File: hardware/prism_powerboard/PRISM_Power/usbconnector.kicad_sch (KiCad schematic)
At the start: 1 part, among them P1 USB_C_Plug

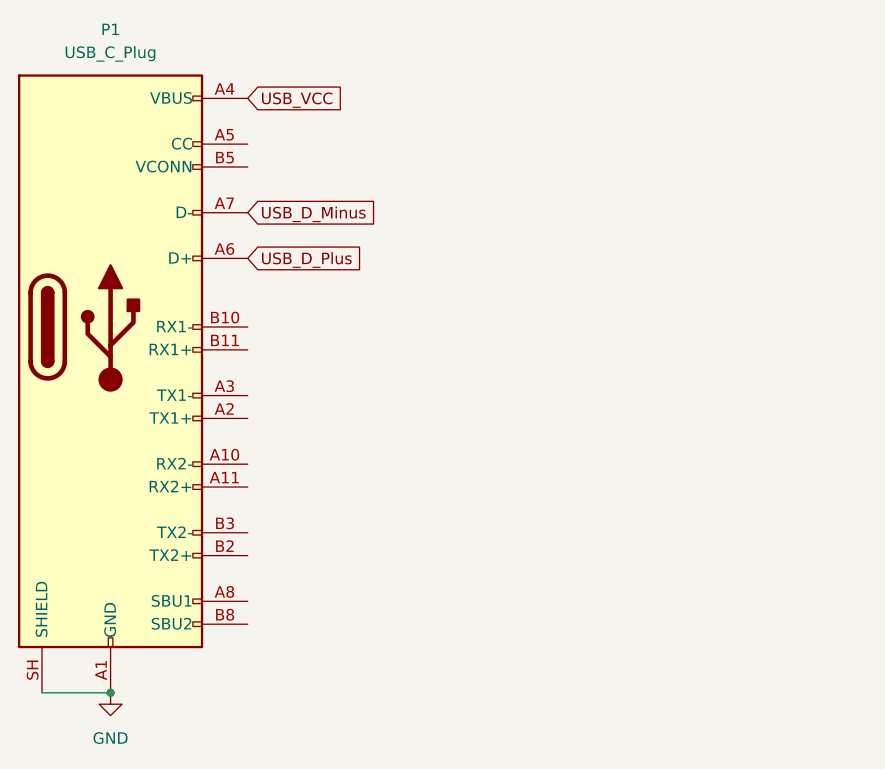
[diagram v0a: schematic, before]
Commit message: Finished Schematics and Start Routing
Finished Schematics and started routing the PCB lines. Added and ensured all footprints were accurate
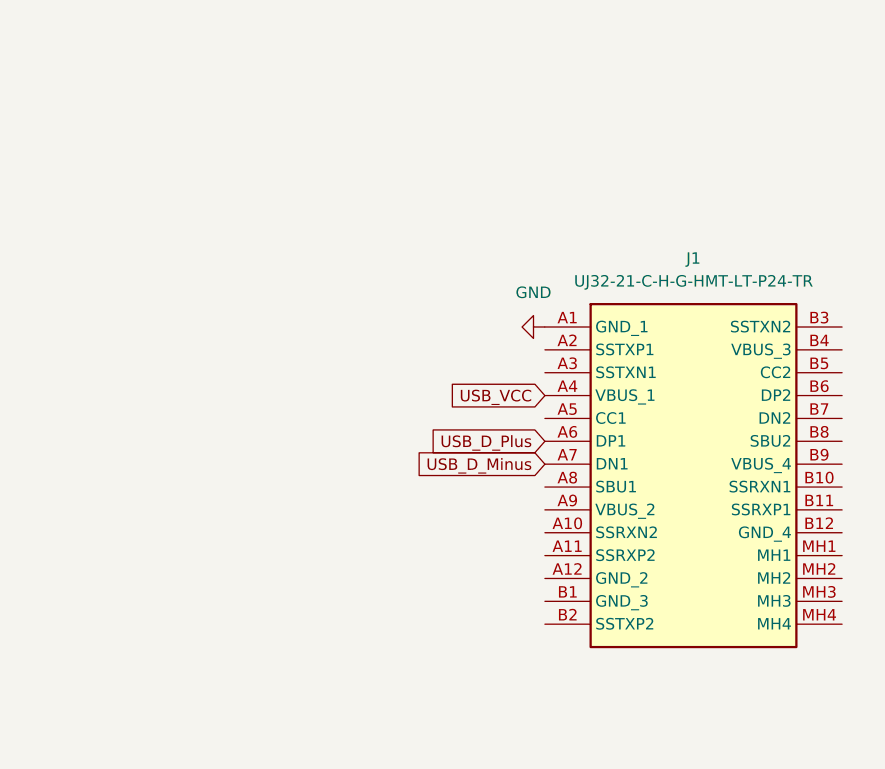
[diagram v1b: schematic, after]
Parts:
- removed P1: USB_C_Plug, Connector_USB:USB_C_Plug_Molex_105444, symbol Connector:USB_C_Plug
- added J1: UJ32-21-C-H-G-HMT-LT-P24-TR, LIB_UJ32-21-C-H-G-HMT-LT-P24-TR:UJ3221CHGHMTLTP24TR, symbol SamacSys:UJ32-21-C-H-G-HMT-LT-P24-TR
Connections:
- net GND: now also J1.A1 (GND_1)
- net USB_D_Minus: now also J1.A7 (DN1)
- net USB_D_Plus: now also J1.A6 (DP1)
- net USB_VCC: now also J1.A4 (VBUS_1)
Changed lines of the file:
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@@
 	(generator_version "10.0")
 	(paper "A4")
-	(junction
-		(at 152.4 116.84)
-		(diameter 0)
-		(color 0 0 0 0)
-	)
-	(wire
-		(pts
-			(xy 144.78 116.84) (xy 152.4 116.84)
-		)
-		(stroke
-			(width 0)
-			(type default)
-		)
-	)
 	(global_label "USB_D_Plus"
 		(shape input)
-		(at 167.64 68.58 0)
+		(at 200.66 88.9 180)
 		(fields_autoplaced yes)
 		(effects
@@
 				(size 1.27 1.27)
 			)
-			(justify left)
+			(justify right)
 		)
 		(property "Intersheetrefs" "${INTERSHEET_REFS}"
-			(at 181.7527 68.58 0)
-			(hide yes)
-			(show_name no)
-			(do_not_autoplace no)
-			(effects
-				(font
-					(size 1.27 1.27)
-				)
-				(justify left)
+			(at 186.5473 88.9 0)
+			(hide yes)
+			(show_name no)
+			(do_not_autoplace no)
+			(effects
+				(font
+					(size 1.27 1.27)
+				)
+				(justify right)
 			)
 		)
@@
 	(global_label "USB_D_Minus"
 		(shape input)
-		(at 167.64 63.5 0)
+		(at 200.66 91.44 180)
 		(fields_autoplaced yes)
 		(effects
@@
 				(size 1.27 1.27)
 			)
-			(justify left)
+			(justify right)
 		)
 		(property "Intersheetrefs" "${INTERSHEET_REFS}"
-			(at 183.0227 63.5 0)
-			(hide yes)
-			(show_name no)
-			(do_not_autoplace no)
-			(effects
-				(font
-					(size 1.27 1.27)
-				)
-				(justify left)
+			(at 185.2773 91.44 0)
+			(hide yes)
+			(show_name no)
+			(do_not_autoplace no)
+			(effects
+				(font
+					(size 1.27 1.27)
+				)
+				(justify right)
 			)
 		)
@@
 	(global_label "USB_VCC"
 		(shape input)
-		(at 167.64 50.8 0)
+		(at 200.66 83.82 180)
 		(fields_autoplaced yes)
 		(effects
@@
 				(size 1.27 1.27)
 			)
-			(justify left)
+			(justify right)
 		)
 		(property "Intersheetrefs" "${INTERSHEET_REFS}"
-			(at 179.0314 50.8 0)
-			(hide yes)
-			(show_name no)
-			(do_not_autoplace no)
-			(effects
-				(font
-					(size 1.27 1.27)
-				)
-				(justify left)
+			(at 189.2686 83.82 0)
+			(hide yes)
+			(show_name no)
+			(do_not_autoplace no)
+			(effects
+				(font
+					(size 1.27 1.27)
+				)
+				(justify right)
 			)
 		)
@@
 	(symbol
 		(lib_id "power:GND")
-		(at 152.4 116.84 0)
+		(at 200.66 76.2 270)
 		(unit 1)
 		(body_style 1)
@@
 		(fields_autoplaced yes)
 		(property "Reference" "#PWR035"
-			(at 152.4 123.19 0)
+			(at 194.31 76.2 0)
 			(hide yes)
 			(show_name no)
@@
 		)
 		(property "Value" "GND"
-			(at 152.4 121.92 0)
+			(at 199.39 72.39 90)
 			(show_name no)
 			(do_not_autoplace no)
@@
 		)
 		(property "Footprint" ""
-			(at 152.4 116.84 0)
+			(at 200.66 76.2 0)
 			(hide yes)
 			(show_name no)
@@
 		)
 		(property "Datasheet" ""
-			(at 152.4 116.84 0)
+			(at 200.66 76.2 0)
 			(hide yes)
 			(show_name no)
@@
 		)
 		(property "Description" "Power symbol creates a global label with name \"GND\" , ground"
-			(at 152.4 116.84 0)
+			(at 200.66 76.2 0)
 			(hide yes)
 			(show_name no)
@@
 	)
 	(symbol
-		(lib_id "Connector:USB_C_Plug")
-		(at 152.4 76.2 0)
+		(lib_id "SamacSys:UJ32-21-C-H-G-HMT-LT-P24-TR")
+		(at 200.66 76.2 0)
 		(unit 1)
 		(body_style 1)
@@
 		(dnp no)
 		(fields_autoplaced yes)
-		(property "Reference" "P1"
-			(at 152.4 43.18 0)
-			(show_name no)
-			(do_not_autoplace no)
-			(effects
-				(font
-					(size 1.27 1.27)
-				)
-			)
-		)
-		(property "Value" "USB_C_Plug"
-			(at 152.4 45.72 0)
-			(show_name no)
-			(do_not_autoplace no)
-			(effects
-				(font
-					(size 1.27 1.27)
-				)
-			)
-		)
-		(property "Footprint" "Connector_USB:USB_C_Plug_Molex_105444"
-			(at 156.21 76.2 0)
-			(hide yes)
-			(show_name no)
-			(do_not_autoplace no)
-			(effects
-				(font
-					(size 1.27 1.27)
-				)
-			)
-		)
-		(property "Datasheet" "https://www.usb.org/sites/default/files/documents/usb_type-c.zip"
-			(at 156.21 76.2 0)
-			(hide yes)
-			(show_name no)
-			(do_not_autoplace no)
-			(effects
-				(font
-					(size 1.27 1.27)
-				)
-			)
-		)
-		(property "Description" "USB Type-C Plug connector"
-			(at 152.4 76.2 0)
-			(hide yes)
-			(show_name no)
-			(do_not_autoplace no)
-			(effects
-				(font
-					(size 1.27 1.27)
-				)
-			)
+		(property "Reference" "J1"
+			(at 217.17 68.58 0)
+			(show_name no)
+			(do_not_autoplace no)
+			(effects
+				(font
+					(size 1.27 1.27)
+				)
+			)
+		)
+		(property "Value" "UJ32-21-C-H-G-HMT-LT-P24-TR"
+			(at 217.17 71.12 0)
+			(show_name no)
+			(do_not_autoplace no)
+			(effects
+				(font
+					(size 1.27 1.27)
+				)
+			)
+		)
+		(property "Footprint" "LIB_UJ32-21-C-H-G-HMT-LT-P24-TR:UJ3221CHGHMTLTP24TR"
+			(at 229.87 171.12 0)
+			(hide yes)
+			(show_name no)
+			(do_not_autoplace no)
+			(effects
+				(font
+					(size 1.27 1.27)
+				)
+				(justify left top)
+			)
+		)
+		(property "Datasheet" "https://www.sameskydevices.com/product/resource/uj32-21-c-h-g-hmt-lt-p24-tr.pdf"
+			(at 229.87 271.12 0)
+			(hide yes)
+			(show_name no)
+			(do_not_autoplace no)
+			(effects
+				(font
+					(size 1.27 1.27)
+				)
+				(justify left top)
+			)
+		)
+		(property "Description" "Type C, USB 3.2 Gen 2x1, 10 Gbps, 20 Vdc, 5 A, Horizontal, Hybrid Mount, Long Anchor Pins, Hybrid Contacts, Gold Flash, 24 Pins, USB Receptacle"
+			(at 200.66 76.2 0)
+			(hide yes)
+			(show_name no)
+			(do_not_autoplace no)
+			(effects
+				(font
+					(size 1.27 1.27)
+				)
+			)
+		)
+		(property "Height" "3.51"
+			(at 229.87 471.12 0)
+			(hide yes)
+			(show_name no)
+			(do_not_autoplace no)
+			(effects
+				(font
+					(size 1.27 1.27)
+				)
+				(justify left top)
+			)
+		)
+		(property "Mouser Part Number" ""
+			(at 229.87 571.12 0)
+			(hide yes)
+			(show_name no)
+			(do_not_autoplace no)
+			(effects
+				(font
+					(size 1.27 1.27)
+				)
+				(justify left top)
+			)
+		)
+		(property "Mouser Price/Stock" ""
+			(at 229.87 671.12 0)
+			(hide yes)
+			(show_name no)
+			(do_not_autoplace no)
+			(effects
+				(font
+					(size 1.27 1.27)
+				)
+				(justify left top)
+			)
+		)
+		(property "Manufacturer_Name" "Same Sky"
+			(at 229.87 771.12 0)
+			(hide yes)
+			(show_name no)
+			(do_not_autoplace no)
+			(effects
+				(font
+					(size 1.27 1.27)
+				)
+				(justify left top)
+			)
+		)
+		(property "Manufacturer_Part_Number" "UJ32-21-C-H-G-HMT-LT-P24-TR"
+			(at 229.87 871.12 0)
+			(hide yes)
+			(show_name no)
+			(do_not_autoplace no)
+			(effects
+				(font
+					(size 1.27 1.27)
+				)
+				(justify left top)
+			)
+		)
+		(pin "A2"
+		)
+		(pin "B2"
 		)
 		(pin "A1"
 		)
+		(pin "MH2"
+		)
+		(pin "A7"
+		)
+		(pin "A12"
+		)
 		(pin "B8"
 		)
+		(pin "B11"
+		)
+		(pin "A4"
+		)
+		(pin "A6"
+		)
+		(pin "A5"
+		)
+		(pin "A10"
+		)
+		(pin "A8"
+		)
+		(pin "B12"
+		)
+		(pin "B5"
+		)
+		(pin "MH1"
+		)
+		(pin "A9"
+		)
+		(pin "B7"
+		)
+		(pin "B4"
+		)
+		(pin "A3"
+		)
+		(pin "B1"
+		)
+		(pin "B9"
+		)
+		(pin "B6"
+		)
+		(pin "A11"
+		)
+		(pin "B10"
+		)
 		(pin "B3"
 		)
-		(pin "SH"
-		)
-		(pin "B10"
-		)
-		(pin "A3"
-		)
-		(pin "B9"
-		)
-		(pin "A4"
-		)
-		(pin "A12"
-		)
-		(pin "A5"
-		)
-		(pin "B5"
-		)
-		(pin "A11"
-		)
-		(pin "B2"
-		)
-		(pin "A9"
-		)
-		(pin "A8"
-		)
-		(pin "B12"
-		)
-		(pin "A10"
-		)
-		(pin "B1"
-		)
-		(pin "A6"
-		)
-		(pin "A2"
-		)
-		(pin "B11"
-		)
-		(pin "B4"
-		)
-		(pin "A7"
+		(pin "MH3"
+		)
+		(pin "MH4"
 		)
 		(instances
 			(project "PRISM_Power"
 				(path "/80548bcf-507c-4ded-a0d2-b94774a2c706/e87287bd-1251-4d75-a949-70cab8f293ec"
-					(reference "P1")
+					(reference "J1")
 					(unit 1)
 				)
